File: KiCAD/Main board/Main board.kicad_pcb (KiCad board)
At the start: 2 copper layers, 190 x 125 mm, 149 parts, among them J1 Conn_01x03, J10 Conn_01x03, J11 Conn_01x03, J12 Conn_01x03, J13 GPIO 0, J14 GPIO 1, J2 Conn_01x03, J3 Conn_01x02, J4 Conn_01x02, J5 Conn_01x03, J6 Conn_01x02, J7 Conn_01x03, J8 Conn_01x02, J9 Conn_01x03, U1 PCM1789, U11 PCM1804, U12 LIN_REG_±5V, U13 LIN_REG_±5V, U14 LIN_REG_±12V, U15 LIN_REG_±12V, U18 12V, U19 5V, U2 LM4562, U20 8V, U21 15V, U3 OPA1632DR, U4 OPA1632DR, U5 OPA1632DR, U7 PCM1804

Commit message: Made symbol and footprint for the FPGA board
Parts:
- removed C44, C45, C51, C56: 100nF, Capacitor_SMD:C_0805_2012Metric
- removed C46, C47, C52, C53, C59, C60: 22uF, Capacitor_THT:CP_Radial_D5.0mm_P2.00mm
- removed C50, C55: 100n, Capacitor_SMD:C_0805_2012Metric
- removed C57, C58: 1n, Capacitor_SMD:C_0805_2012Metric
- removed C61: 2.7n, Capacitor_SMD:C_0805_2012Metric
- removed J13: GPIO 0, Connector_IDC:IDC-Header_2x20_P2.54mm_Vertical
- removed J14: GPIO 1, Connector_IDC:IDC-Header_2x20_P2.54mm_Vertical
- removed R50, R51, R57, R58, R64, R65: 10, Resistor_SMD:R_0805_2012Metric
- removed R62: 1k, Resistor_SMD:R_0805_2012Metric
- removed R66: 270, Resistor_SMD:R_0805_2012Metric
- removed R69, R70: 39, Resistor_SMD:R_0805_2012Metric
- removed U11: PCM1804, Package_SO:SSOP-28_5.3x10.2mm_P0.65mm
- added U8: ~, Audio-DSP:DE1-SoC, F.Cu at (70.6, 176.9)
- moved H7 10.0 mm to (100.0, 165.0)

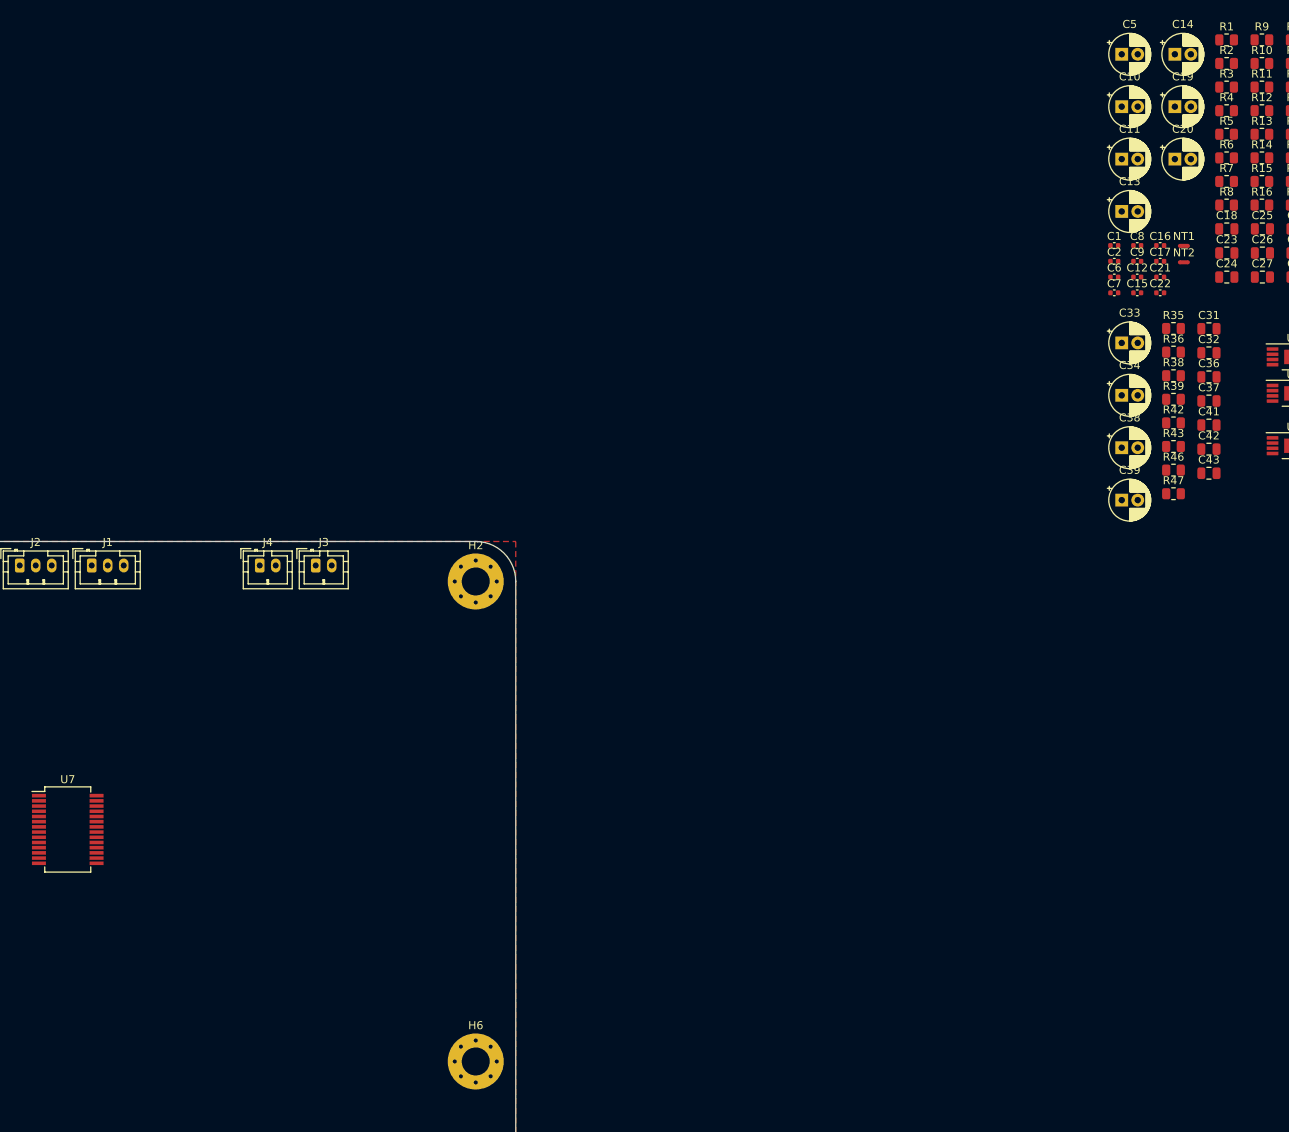
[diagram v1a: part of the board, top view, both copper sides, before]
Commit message: Added SEPIC symbol and footprint and worked on main board
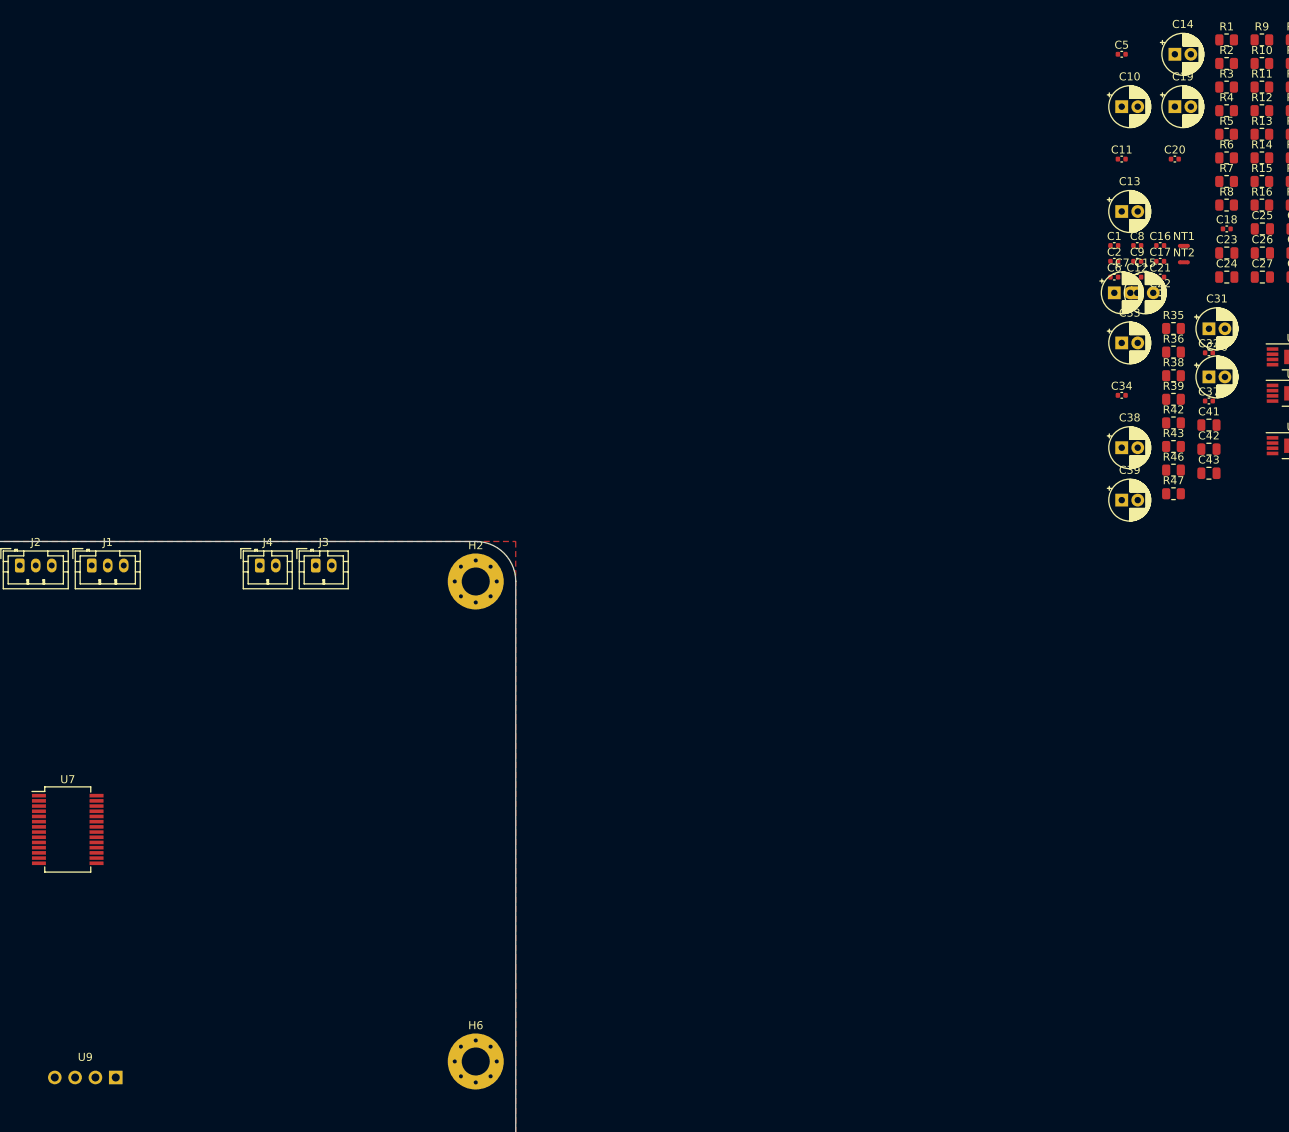
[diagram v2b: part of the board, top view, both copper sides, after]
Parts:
- added U9: SEPIC_-15V_LT3579, Audio-DSP:SEPIC_-15V_LT3579, F.Cu at (186.2, 167.0)
- C11, C20, C34, C5: value 22uF -> 100n; footprint Capacitor_THT:CP_Radial_D5.0mm_P2.00mm -> Capacitor_SMD:C_0402_1005Metric
- C15, C7: value 100n -> 22uF; footprint Capacitor_SMD:C_0402_1005Metric -> Capacitor_THT:CP_Radial_D5.0mm_P2.00mm
- C18: footprint Capacitor_SMD:C_0805_2012Metric -> Capacitor_SMD:C_0402_1005Metric
- C29, C30: value 2.2n -> 2n2
- C31: value 100nF -> 22uF; footprint Capacitor_SMD:C_0805_2012Metric -> Capacitor_THT:CP_Radial_D5.0mm_P2.00mm
- C32, C37: value 100nF -> 100n; footprint Capacitor_SMD:C_0805_2012Metric -> Capacitor_SMD:C_0402_1005Metric
- C36: value 100n -> 22uF; footprint Capacitor_SMD:C_0805_2012Metric -> Capacitor_THT:CP_Radial_D5.0mm_P2.00mm
- R17, R18, R19, R20: value 4.7k -> 4k7
- R25, R27: value 4.3K -> 4k3
- R26, R28: value 4.3k -> 4k3
- R35, R36, R38, R39: value 10 -> 10R
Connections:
- C10 pad 1: Net-(U3B-V+) -> GND
- C10 pad 2: GND -> Net-(U3B-V-)
- C11 pad 1: GND -> Net-(U4B-V+)
- C11 pad 2: Net-(U3B-V-) -> GND
- C19 pad 1: Net-(U4B-V+) -> GND
- C19 pad 2: GND -> Net-(U4B-V-)
- C20 pad 1: GND -> Net-(U5B-V+)
- C20 pad 2: Net-(U4B-V-) -> GND
- C33 pad 1: Net-(U5B-V+) -> GND
- C33 pad 2: GND -> Net-(U5B-V-)
- C34 pad 1: GND -> Net-(U6C-V+)
- C34 pad 2: Net-(U5B-V-) -> GND
- C38 pad 1: Net-(U6C-V+) -> GND
- C38 pad 2: GND -> Net-(U6C-V-)
- C39 pad 1: GND -> +3.3V
- C39 pad 2: Net-(U6C-V-) -> GND
- C6 pad 1: +3.3V -> Net-(U3B-V+)
- R35 pad 1: Net-(U5B-V+) -> +12V
- R35 pad 2: +12V -> Net-(U5B-V+)
- R36 pad 1: -12V -> Net-(U5B-V-)
- R36 pad 2: Net-(U5B-V-) -> -12V
- R38 pad 1: Net-(U6C-V+) -> +12V
- R38 pad 2: +12V -> Net-(U6C-V+)
- R39 pad 1: -12V -> Net-(U6C-V-)
- R39 pad 2: Net-(U6C-V-) -> -12V

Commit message: Worked on main board and added nettie 0.3mm
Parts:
- NT1, NT2: footprint NetTie:NetTie-2_SMD_Pad0.5mm -> Audio-DSP:NetTie-2_SMD_Pad0.3mm
- moved NT1 210.7 mm to (115.8, 98.0)
- moved NT2 7.10 mm to (323.8, 58.0)
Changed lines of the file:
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@@
     )
   )
+  (footprint "Audio-DSP:NetTie-2_SMD_Pad0.3mm" (layer "F.Cu")
+    (at 115.75 98)
+    (property "Sheetfile" "DAC_CH1_2.kicad_sch")
+    (property "Sheetname" "DAC_CH1_2")
+    (property "exclude_from_bom" "")
+    (property "ki_description" "Net tie, 2 pins")
+    (property "ki_keywords" "net tie short")
+    (attr smd exclude_from_bom)
+    (fp_text reference "NT1" (at 0 -0.5 unlocked) (layer "F.SilkS") hide
+        (effects (font (size 1 1) (thickness 0.1)))
+    )
+    (fp_text value "NetTie_2" (at 0 1 unlocked) (layer "F.Fab")
+        (effects (font (size 1 1) (thickness 0.15)))
+    )
+    (fp_text user "${REFERENCE}" (at 0 2.5 unlocked) (layer "F.Fab")
+        (effects (font (size 1 1) (thickness 0.15)))
+    )
+    (fp_poly
+      (pts
+        (xy -0.25 -0.15)
+        (xy 0.25 -0.15)
+        (xy 0.25 0.15)
+        (xy -0.25 0.15)
+      )
+      (stroke (width 0) (type solid)) (fill solid) (layer "F.Cu"))
+    (fp_line (start -0.45 -0.2) (end -0.45 0.2)
+      (stroke (width 0.05) (type solid)) (layer "F.CrtYd"))
+    (fp_line (start -0.45 0.2) (end 0.45 0.2)
+      (stroke (width 0.05) (type solid)) (layer "F.CrtYd"))
+    (fp_line (start 0.45 -0.2) (end -0.45 -0.2)
+      (stroke (width 0.05) (type solid)) (layer "F.CrtYd"))
+    (fp_line (start 0.45 0.2) (end 0.45 -0.2)
+      (stroke (width 0.05) (type solid)) (layer "F.CrtYd"))
+    (pad "1" smd circle (at -0.25 0) (size 0.3 0.3) (layers "F.Cu")
+      (net 2 "GND") (pinfunction "1") (pintype "passive"))
+    (pad "2" smd circle (at 0.25 0) (size 0.3 0.3) (layers "F.Cu")
+      (net 15 "/DAC_CH1_2/RCA_JACK_CH1(REF)") (pinfunction "2") (pintype "passive"))
+  )
   (footprint "Capacitor_THT:CP_Radial_D5.0mm_P2.00mm" (layer "F.Cu")
     (at 322.38705 39.1)
@@
     )
   )
-  (footprint "NetTie:NetTie-2_SMD_Pad0.5mm" (layer "F.Cu")
-    (at 323.5175 63.05)
-    (descr "Net tie, 2 pin, 0.5mm square SMD pads")
-    (tags "net tie")
-    (property "Sheetfile" "DAC_CH1_2.kicad_sch")
-    (property "Sheetname" "DAC_CH1_2")
-    (property "exclude_from_bom" "")
-    (property "ki_description" "Net tie, 2 pins")
-    (property "ki_keywords" "net tie short")
-    (attr exclude_from_pos_files exclude_from_bom)
-    (net_tie_pad_groups "1, 2")
-    (fp_text reference "NT1" (at 0 -1.2) (layer "F.SilkS")
-        (effects (font (size 1 1) (thickness 0.15)))
-    )
-    (fp_text value "NetTie_2" (at 0 1.2) (layer "F.Fab")
-        (effects (font (size 1 1) (thickness 0.15)))
-    )
-    (fp_poly
-      (pts
-        (xy -0.5 -0.25)
-        (xy 0.5 -0.25)
-        (xy 0.5 0.25)
-        (xy -0.5 0.25)
-      )
-      (stroke (width 0) (type solid)) (fill solid) (layer "F.Cu"))
-    (fp_line (start -1 -0.5) (end -1 0.5)
-      (stroke (width 0.05) (type solid)) (layer "F.CrtYd"))
-    (fp_line (start -1 0.5) (end 1 0.5)
-      (stroke (width 0.05) (type solid)) (layer "F.CrtYd"))
-    (fp_line (start 1 -0.5) (end -1 -0.5)
-      (stroke (width 0.05) (type solid)) (layer "F.CrtYd"))
-    (fp_line (start 1 0.5) (end 1 -0.5)
-      (stroke (width 0.05) (type solid)) (layer "F.CrtYd"))
-    (pad "1" smd circle (at -0.5 0) (size 0.5 0.5) (layers "F.Cu")
-      (net 2 "GND") (pinfunction "1") (pintype "passive"))
-    (pad "2" smd circle (at 0.5 0) (size 0.5 0.5) (layers "F.Cu")
-      (net 15 "/DAC_CH1_2/RCA_JACK_CH1(REF)") (pinfunction "2") (pintype "passive"))
-  )
   (footprint "Capacitor_SMD:C_0402_1005Metric" (layer "F.Cu")
     (at 320.5575 64.98)
@@
     )
   )
-  (footprint "NetTie:NetTie-2_SMD_Pad0.5mm" (layer "F.Cu")
-    (at 323.5175 65.1)
-    (descr "Net tie, 2 pin, 0.5mm square SMD pads")
-    (tags "net tie")
-    (property "Sheetfile" "DAC_CH1_2.kicad_sch")
-    (property "Sheetname" "DAC_CH1_2")
-    (property "exclude_from_bom" "")
-    (property "ki_description" "Net tie, 2 pins")
-    (property "ki_keywords" "net tie short")
-    (attr exclude_from_pos_files exclude_from_bom)
-    (net_tie_pad_groups "1, 2")
-    (fp_text reference "NT2" (at 0 -1.2) (layer "F.SilkS")
-        (effects (font (size 1 1) (thickness 0.15)))
-    )
-    (fp_text value "NetTie_2" (at 0 1.2) (layer "F.Fab")
-        (effects (font (size 1 1) (thickness 0.15)))
-    )
-    (fp_poly
-      (pts
-        (xy -0.5 -0.25)
-        (xy 0.5 -0.25)
-        (xy 0.5 0.25)
-        (xy -0.5 0.25)
-      )
-      (stroke (width 0) (type solid)) (fill solid) (layer "F.Cu"))
-    (fp_line (start -1 -0.5) (end -1 0.5)
-      (stroke (width 0.05) (type solid)) (layer "F.CrtYd"))
-    (fp_line (start -1 0.5) (end 1 0.5)
-      (stroke (width 0.05) (type solid)) (layer "F.CrtYd"))
-    (fp_line (start 1 -0.5) (end -1 -0.5)
-      (stroke (width 0.05) (type solid)) (layer "F.CrtYd"))
-    (fp_line (start 1 0.5) (end 1 -0.5)
-      (stroke (width 0.05) (type solid)) (layer "F.CrtYd"))
-    (pad "1" smd circle (at -0.5 0) (size 0.5 0.5) (layers "F.Cu")
-      (net 2 "GND") (pinfunction "1") (pintype "passive"))
-    (pad "2" smd circle (at 0.5 0) (size 0.5 0.5) (layers "F.Cu")
-      (net 31 "/DAC_CH1_2/RCA_JACK_CH2(REF)") (pinfunction "2") (pintype "passive"))
-  )
   (footprint "Resistor_SMD:R_0805_2012Metric" (layer "F.Cu")
     (at 337.6775 40.25)
@@
     )
   )
+  (footprint "Audio-DSP:NetTie-2_SMD_Pad0.3mm" (layer "F.Cu")
+    (at 323.75 58)
+    (property "Sheetfile" "DAC_CH1_2.kicad_sch")
+    (property "Sheetname" "DAC_CH1_2")
+    (property "exclude_from_bom" "")
+    (property "ki_description" "Net tie, 2 pins")
+    (property "ki_keywords" "net tie short")
+    (attr smd exclude_from_bom)
+    (fp_text reference "NT2" (at 0 -0.5 unlocked) (layer "F.SilkS") hide
+        (effects (font (size 1 1) (thickness 0.1)))
+    )
+    (fp_text value "NetTie_2" (at 0 1 unlocked) (layer "F.Fab")
+        (effects (font (size 1 1) (thickness 0.15)))
+    )
+    (fp_text user "${REFERENCE}" (at 0 2.5 unlocked) (layer "F.Fab")
+        (effects (font (size 1 1) (thickness 0.15)))
+    )
+    (fp_poly
+      (pts
+        (xy -0.25 -0.15)
+        (xy 0.25 -0.15)
+        (xy 0.25 0.15)
+        (xy -0.25 0.15)
+      )
+      (stroke (width 0) (type solid)) (fill solid) (layer "F.Cu"))
+    (fp_line (start -0.45 -0.2) (end -0.45 0.2)
+      (stroke (width 0.05) (type solid)) (layer "F.CrtYd"))
+    (fp_line (start -0.45 0.2) (end 0.45 0.2)
+      (stroke (width 0.05) (type solid)) (layer "F.CrtYd"))
+    (fp_line (start 0.45 -0.2) (end -0.45 -0.2)
+      (stroke (width 0.05) (type solid)) (layer "F.CrtYd"))
+    (fp_line (start 0.45 0.2) (end 0.45 -0.2)
+      (stroke (width 0.05) (type solid)) (layer "F.CrtYd"))
+    (pad "1" smd circle (at -0.25 0) (size 0.3 0.3) (layers "F.Cu")
+      (net 2 "GND") (pinfunction "1") (pintype "passive"))
+    (pad "2" smd circle (at 0.25 0) (size 0.3 0.3) (layers "F.Cu")
+      (net 31 "/DAC_CH1_2/RCA_JACK_CH2(REF)") (pinfunction "2") (pintype "passive"))
+  )
   (footprint "Capacitor_SMD:C_0402_1005Metric" (layer "F.Cu")
     (at 317.6875 63.01)
@@
     (property "ki_description" "DE1-SoC FPGA")
     (attr through_hole)
-    (fp_text reference "U8" (at -2 -48.6 unlocked) (layer "F.SilkS") hide
+    (fp_text reference "U8" (at 0.43 -1.87 unlocked) (layer "F.SilkS") hide
         (effects (font (size 1 1) (thickness 0.1)))
     )
@@
         (effects (font (size 1.5 1.5) (thickness 0.3) bold) (justify left bottom))
     )
-    (fp_text user "${REFERENCE}" (at 0 1.27 unlocked) (layer "F.Fab")
-        (effects (font (size 1 1) (thickness 0.15)))
-    )
     (fp_text user "${REFERENCE}" (at -10.16 0 -90) (layer "F.Fab")
